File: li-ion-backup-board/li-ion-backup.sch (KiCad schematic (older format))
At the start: 70 parts

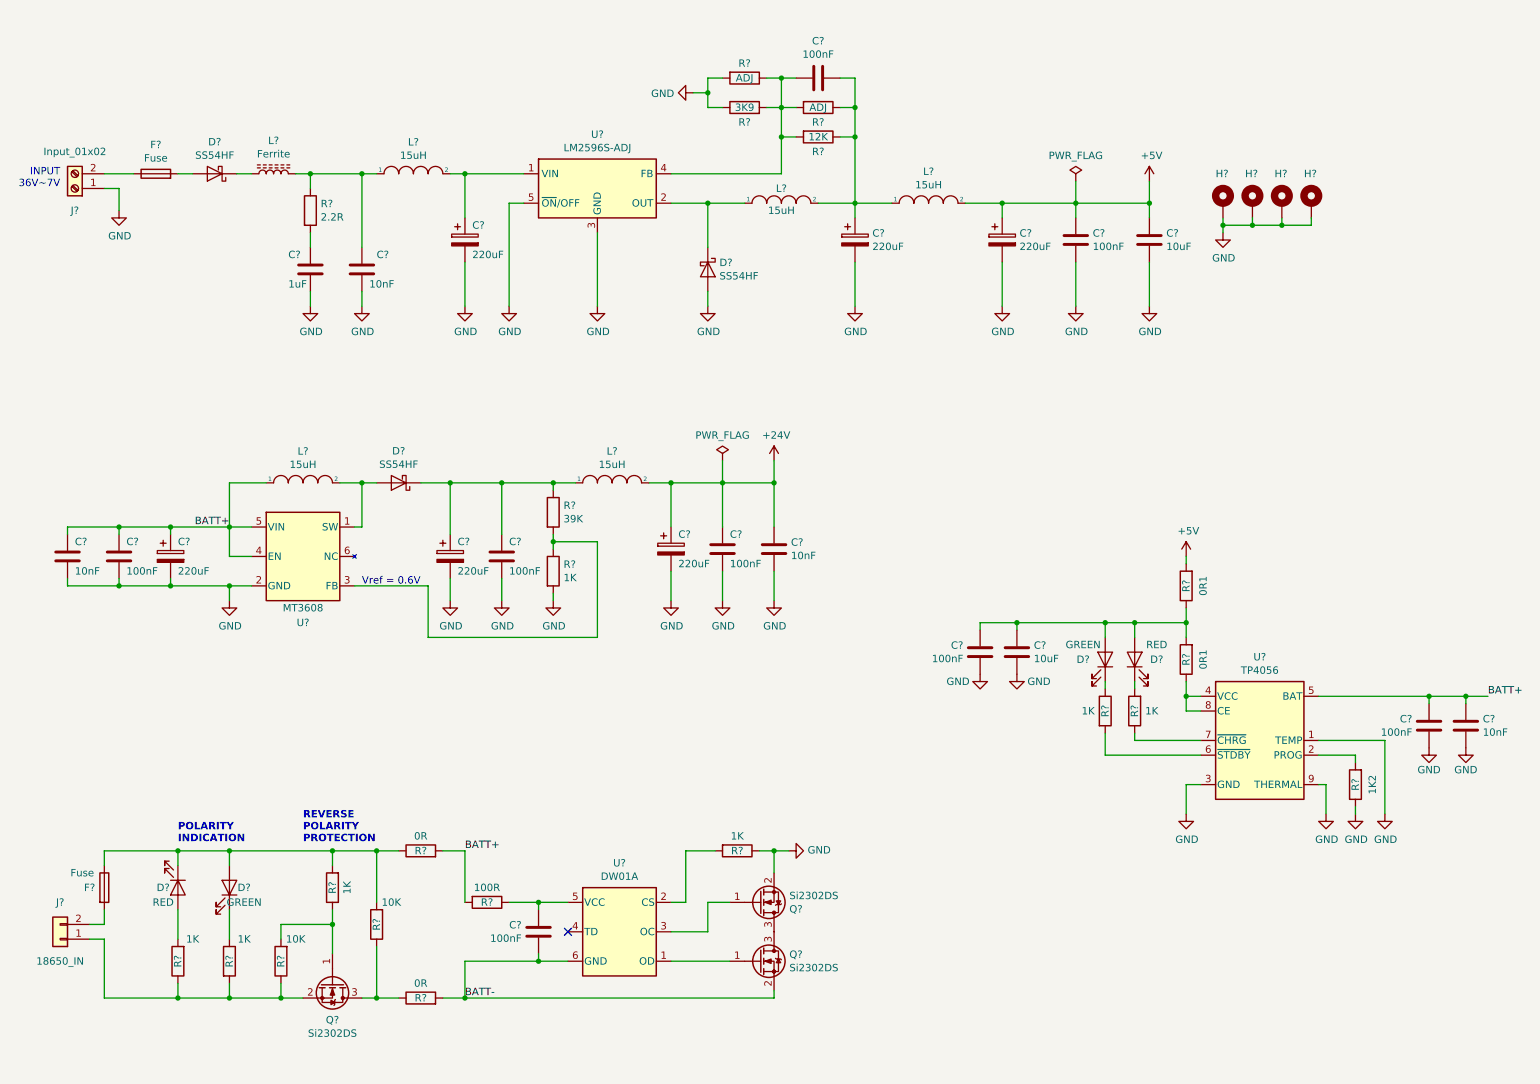
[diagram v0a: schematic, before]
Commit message: edge cuts corrigido
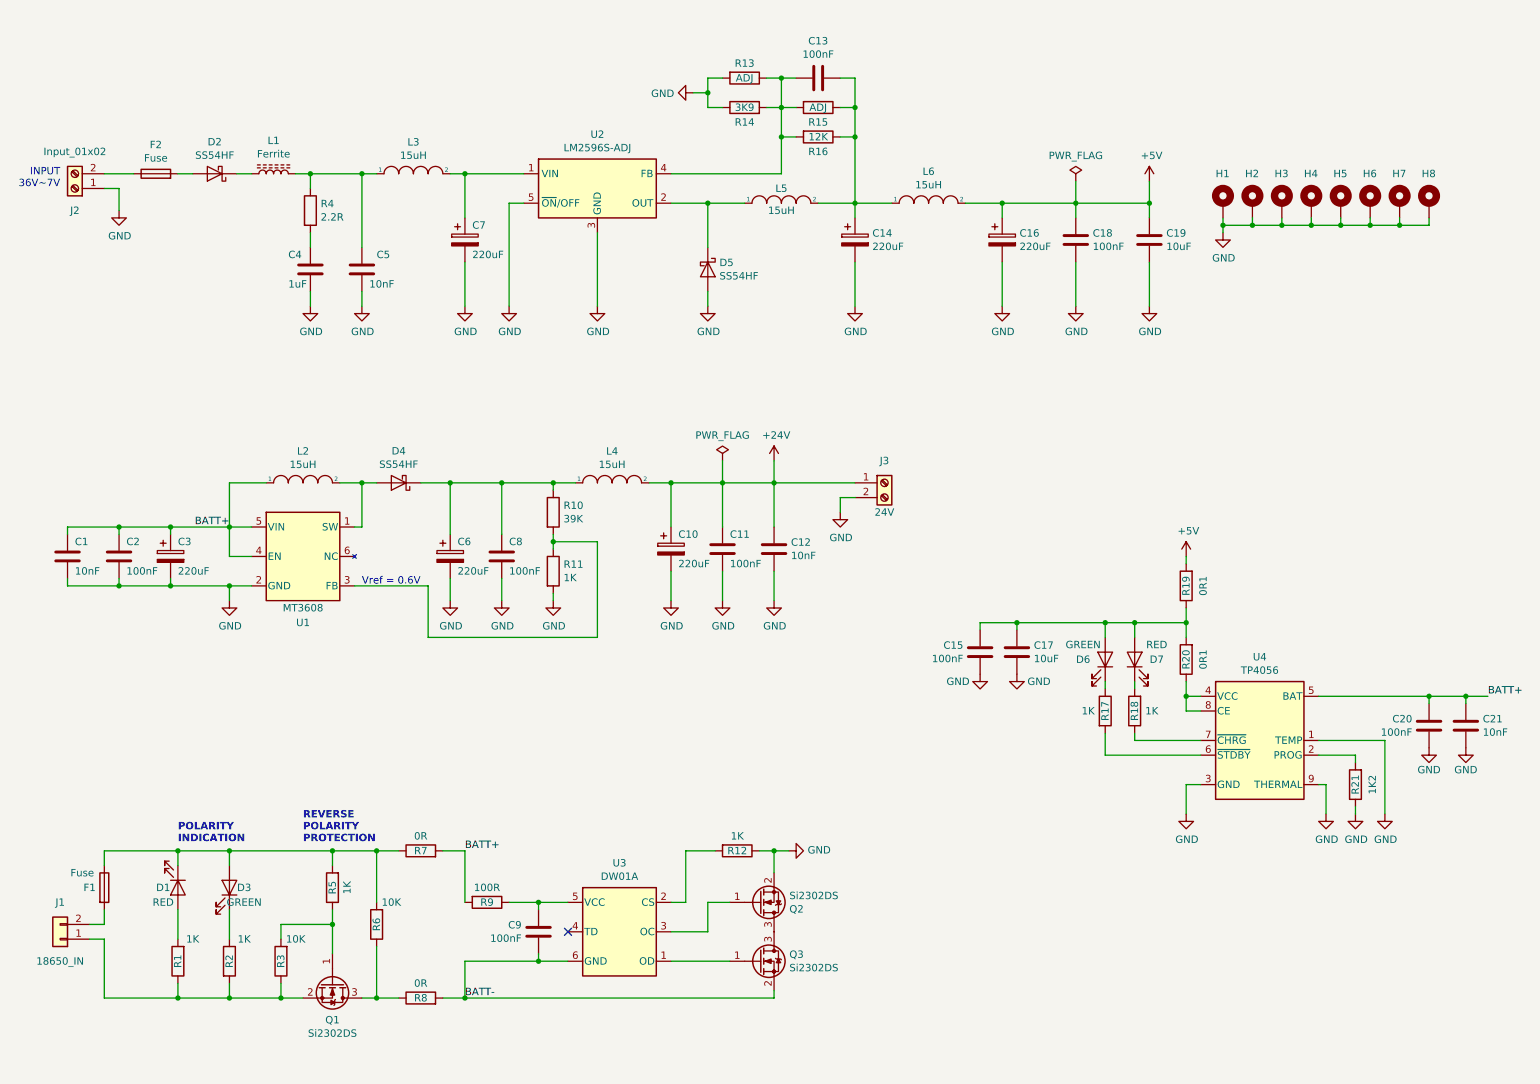
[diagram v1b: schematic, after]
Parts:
- added H5, H6, H7, H8: MountingHole_Pad, MountingHole:MountingHole_3.2mm_M3_Pad_Via, symbol Mechanical:MountingHole_Pad
- added J3: 24V, e-Power:TerminalBlock_Phoenix_MKDS-1,5-2_1x02_P5.08mm_Horizontal_3D, symbol Connector:Screw_Terminal_01x02
- H1, H2, H3, H4: renamed from H?; footprint (none) -> MountingHole:MountingHole_3.2mm_M3_Pad_Via
- J1: renamed from J?; footprint (none) -> e-Power:BatteryHolder_1x18650
- gave numbers to parts that had none: 65
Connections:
- net +24V: now also J3.1 (Pin_1)
- net GND: now also H5.1, H6.1, H7.1, H8.1, J3.2 (Pin_2)

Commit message: add gerbers and production files
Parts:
- added F3, F4, F5, F6, F7: Fuse, e-Power:FUSE_1206_3216Metric, symbol Device:Fuse
- added J4: OUT_SIG, e-Power:TerminalBlock_Phoenix_MKDS-1,5-2_1x02_P5.08mm_Horizontal_3D, symbol Connector:Screw_Terminal_01x02
- added Q4: MMBT5551, Package_TO_SOT_SMD:SOT-23, symbol Transistor_BJT:MMBT5550L
- added Q5: MMBT5401, Package_TO_SOT_SMD:SOT-23, symbol Transistor_BJT:MMBT3906
- added R22, R24, R25, R26, R27: 10K, Resistor_SMD:R_0805_2012Metric, symbol Device:R
- added R23, R28: 1K, Resistor_SMD:R_0805_2012Metric, symbol Device:R
- added TP1: BATT+, e-Power:TestPoint_Pad_D1.0mm, symbol Connector:TestPoint
- added TP10, TP11, TP9: GND, e-Power:TestPoint_Pad_D1.0mm, symbol Connector:TestPoint
- added TP2: BATT-, e-Power:TestPoint_Pad_D1.0mm, symbol Connector:TestPoint
- added TP3: VIN, e-Power:TestPoint_Pad_D1.0mm, symbol Connector:TestPoint
- added TP4: 0.6V, e-Power:TestPoint_Pad_D1.0mm, symbol Connector:TestPoint
- added TP5: 1.2V, e-Power:TestPoint_Pad_D1.0mm, symbol Connector:TestPoint
- added TP6: 24V, e-Power:TestPoint_Pad_D1.0mm, symbol Connector:TestPoint
- added TP7: SIG, e-Power:TestPoint_Pad_D1.0mm, symbol Connector:TestPoint
- added TP8: 5V, e-Power:TestPoint_Pad_D1.0mm, symbol Connector:TestPoint
- L2, L3, L4, L5, L6: value 15uH -> 10uH; LCSC C151872 -> C9935
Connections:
- net +24V: now also J3.2 (Pin_2), J4.2 (Pin_2), Q5.2 (E), R26.2, R27.2, TP6.1; no longer J3.1 (Pin_1)
- net +5V: now also R28.2, TP8.1
- net GND: now also J3.1 (Pin_1), R2.2, F3.2, F4.2, F5.2, F6.2, F7.2, Q4.2 (E), R23.2, R25.2, R26.1, R27.1, R28.1, TP10.1, TP11.1, TP9.1; no longer J3.2 (Pin_2)
- net VIN: now reaches C7.1, L3.2, U2.1 (VIN)
- net VIN: now also R22.1, TP3.1
- net at C13.2, R13.1, R14.2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: now also TP5.1
- net at D1.1 (K), D3.2 (A), F1.1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: now also TP1.1
- net at F1.2: now also J1.1 (Pin_1); no longer J1.2 (Pin_2)
- net at Q1.2 (S), R1.1, R3.1: now also J1.2 (Pin_2); no longer J1.1 (Pin_1), R2.2
- net at Q1.3 (D), R6.1, R8.1: now also TP2.1
- net at R10.2, R11.1, U1.3 (FB): now also TP4.1
- new net: J4.1 (Pin_1), Q5.3 (C), R25.1, TP7.1
- new net: Q5.1 (B), R24.1
- new net: Q4.1 (B), R22.2, R23.1
- new net: Q4.3 (C), R24.2
- new net: F3.1, F4.1, F5.1, F6.1, F7.1
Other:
- note added: "0 -> NO POWER DETECTED\n1 -> POWER CONNECTED"
- note added: "EXTRA FUSES"
- moved on the sheet: C1, C10, C11, C12, C2, C3, C6, C8, D4, H1, H2, H3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

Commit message: teste
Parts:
- U1: LCSC C84817 -> C78162
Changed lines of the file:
@@
 F 2 "Package_TO_SOT_SMD:SOT-23-6" H 2400 2875 50  0001 C CIN
 F 3 "https://datasheet.lcsc.com/szlcsc/XI-AN-Aerosemi-Tech-MT3608_C84817.pdf" H 2400 3500 50  0001 C CNN
-F 4 "C84817" H 2400 2950 50  0001 C CNN "LCSC"
+F 4 "C78162" H 2400 2950 50  0001 C CNN "LCSC"
 	1    2400 3550
 	1    0    0    -1
